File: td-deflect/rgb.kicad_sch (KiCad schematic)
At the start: 2 parts, among them J2 Conn_01x07_Male, J3 Conn_01x05_Pin

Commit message: more layout
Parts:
- added TH1: Polyfuse, Fuse:Fuse_0805_2012Metric, symbol Device:Polyfuse
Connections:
- net +12V: now also TH1.2; no longer J2.2 (Pin_2)
- new net +12v_sync: J2.2 (Pin_2), TH1.1
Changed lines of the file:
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@@
 (kicad_sch (version 20230121) (generator eeschema)
   (paper "A4")
-  (wire (pts (xy 162.56 107.95) (xy 148.59 107.95))
+  (wire (pts (xy 148.59 107.95) (xy 165.1 107.95))
     (stroke (width 0) (type default))
+  )
+  (label "+12v_sync" (at 153.67 107.95 0) (fields_autoplaced)
+    (effects (font (size 1.27 1.27)) (justify left bottom))
   )
   (global_label "SEP_OE" (shape input) (at 148.59 115.57 0) (fields_autoplaced)
@@
     )
   )
-  (symbol (lib_id "power:+12V") (at 162.56 107.95 270) (unit 1)
+  (symbol (lib_id "power:+12V") (at 172.72 107.95 270) (unit 1)
     (in_bom yes) (on_board yes) (dnp no)
-    (property "Reference" "#PWR024" (at 158.75 107.95 0)
+    (property "Reference" "#PWR024" (at 168.91 107.95 0)
       (effects (font (size 1.27 1.27)) hide)
     )
-    (property "Value" "+12V" (at 166.9542 108.331 0)
+    (property "Value" "+12V" (at 177.1142 108.331 0)
       (effects (font (size 1.27 1.27)))
     )
-    (property "Footprint" "" (at 162.56 107.95 0)
+    (property "Footprint" "" (at 172.72 107.95 0)
       (effects (font (size 1.27 1.27)) hide)
     )
-    (property "Datasheet" "" (at 162.56 107.95 0)
+    (property "Datasheet" "" (at 172.72 107.95 0)
       (effects (font (size 1.27 1.27)) hide)
     )
@@
         )
       )
+    )
+  )
+  (symbol (lib_id "Device:Polyfuse") (at 168.91 107.95 90) (unit 1)
+    (in_bom yes) (on_board yes) (dnp no) (fields_autoplaced)
+    (property "Reference" "TH1" (at 168.91 102.4087 90)
+      (effects (font (size 1.27 1.27)))
+    )
+    (property "Value" "Polyfuse" (at 168.91 104.8329 90)
+      (effects (font (size 1.27 1.27)))
+    )
+    (property "Footprint" "Fuse:Fuse_0805_2012Metric" (at 173.99 106.68 0)
+      (effects (font (size 1.27 1.27)) (justify left) hide)
+    )
+    (property "Datasheet" "~" (at 168.91 107.95 0)
+      (effects (font (size 1.27 1.27)) hide)
+    )
+    (pin "2")
+    (pin "1")
+    (instances
+      (project "td-deflect"
+        (path "/55a1a5e1-4d11-4c3e-b2b4-b9d50ddc5f9d/00000000-0000-0000-0000-00005dbce206"
+          (reference "TH1") (unit 1)
+        )
+      )

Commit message: update pcb
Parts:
- J3: Digikey B5B-XH-A -> 455-B5B-XH-A-ND
- TH1: Digikey (none) -> 507-1801-1-ND
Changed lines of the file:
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@@
+      (effects (font (size 1.27 1.27)) hide)
+    )
+    (property "Digikey" "507-1801-1-ND" (at 168.91 107.95 0)
       (effects (font (size 1.27 1.27)) hide)
     )
@@
       (effects (font (size 1.27 1.27)) hide)
     )
-    (property "Digikey" "B5B-XH-A" (at 115.57 109.22 0)
+    (property "Digikey" "455-B5B-XH-A-ND" (at 115.57 109.22 0)
       (effects (font (size 1.27 1.27)) hide)
     )

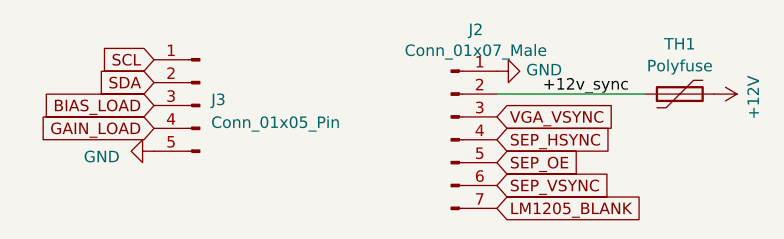
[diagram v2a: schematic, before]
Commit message: update td-deflect kicad version
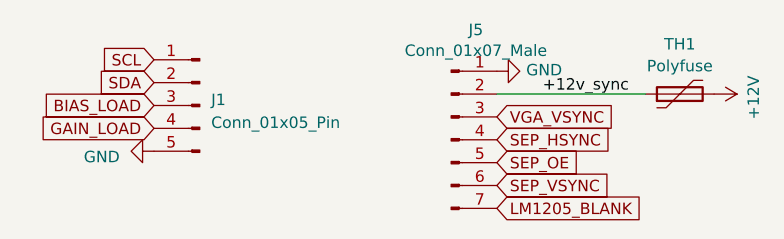
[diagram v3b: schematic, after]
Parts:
- renumbered J3 to J1, J2 to J5

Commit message: shrink board a lot
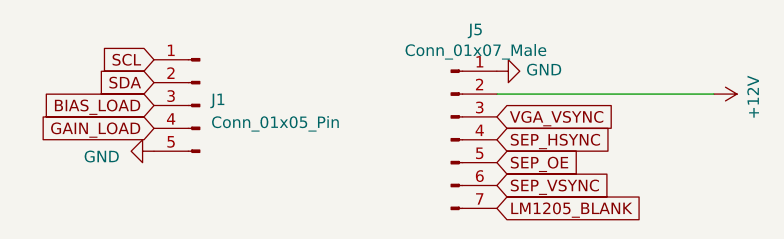
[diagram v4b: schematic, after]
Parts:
- removed TH1: Polyfuse, Fuse:Fuse_0805_2012Metric, symbol Device:Polyfuse
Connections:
- net +12v_sync is gone; now on net +12V: J5.2 (Pin_2)
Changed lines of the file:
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@@
 	(wire
 		(pts
-			(xy 148.59 107.95) (xy 165.1 107.95)
+			(xy 148.59 107.95) (xy 172.72 107.95)
 		)
 		(stroke
 			(width 0)
 			(type default)
-		)
-	)
-	(label "+12v_sync"
-		(at 153.67 107.95 0)
-		(effects
-			(font
-				(size 1.27 1.27)
-			)
-			(justify left bottom)
 		)
 	)
@@
 					(unit 1)
 				)
-			)
-		)
-	)
-	(symbol
-		(lib_id "Device:Polyfuse")
-		(at 168.91 107.95 90)
-		(unit 1)
-		(exclude_from_sim no)
-		(in_bom yes)
-		(on_board yes)
-		(dnp no)
-		(fields_autoplaced yes)
-		(property "Reference" "TH1"
-			(at 168.91 102.4087 90)
-			(effects
-				(font
-					(size 1.27 1.27)
-				)
-			)
-		)
-		(property "Value" "Polyfuse"
-			(at 168.91 104.8329 90)
-			(effects
-				(font
-					(size 1.27 1.27)
-				)
-			)
-		)
-		(property "Footprint" "Fuse:Fuse_0805_2012Metric"
-			(at 173.99 106.68 0)
-			(effects
-				(font
-					(size 1.27 1.27)
-				)
-				(justify left)
-				(hide yes)
-			)
-		)
-		(property "Datasheet" "~"
-			(at 168.91 107.95 0)
-			(effects
-				(font
-					(size 1.27 1.27)
-				)
-				(hide yes)
-			)
-		)
-		(property "Description" ""
-			(at 168.91 107.95 0)
-			(effects
-				(font
-					(size 1.27 1.27)
-				)
-			)
-		)
-		(property "Digikey" "507-1801-1-ND"
-			(at 168.91 107.95 0)
-			(effects
-				(font
-					(size 1.27 1.27)
-				)
-				(hide yes)
-			)
-		)
-		(pin "2"
-		)
-		(pin "1"
-		)
-		(instances
-			(project "td-deflect"
-				(path "/55a1a5e1-4d11-4c3e-b2b4-b9d50ddc5f9d/00000000-0000-0000-0000-00005dbce206"
-					(reference "TH1")
-					(unit 1)
-				)
